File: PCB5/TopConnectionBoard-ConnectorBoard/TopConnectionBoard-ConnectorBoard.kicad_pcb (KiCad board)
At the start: 2 copper layers, 51 x 50 mm, 8 parts, among them P1 CONN1, P2 CONN2, P3 CONN_A, P4 CONN_B

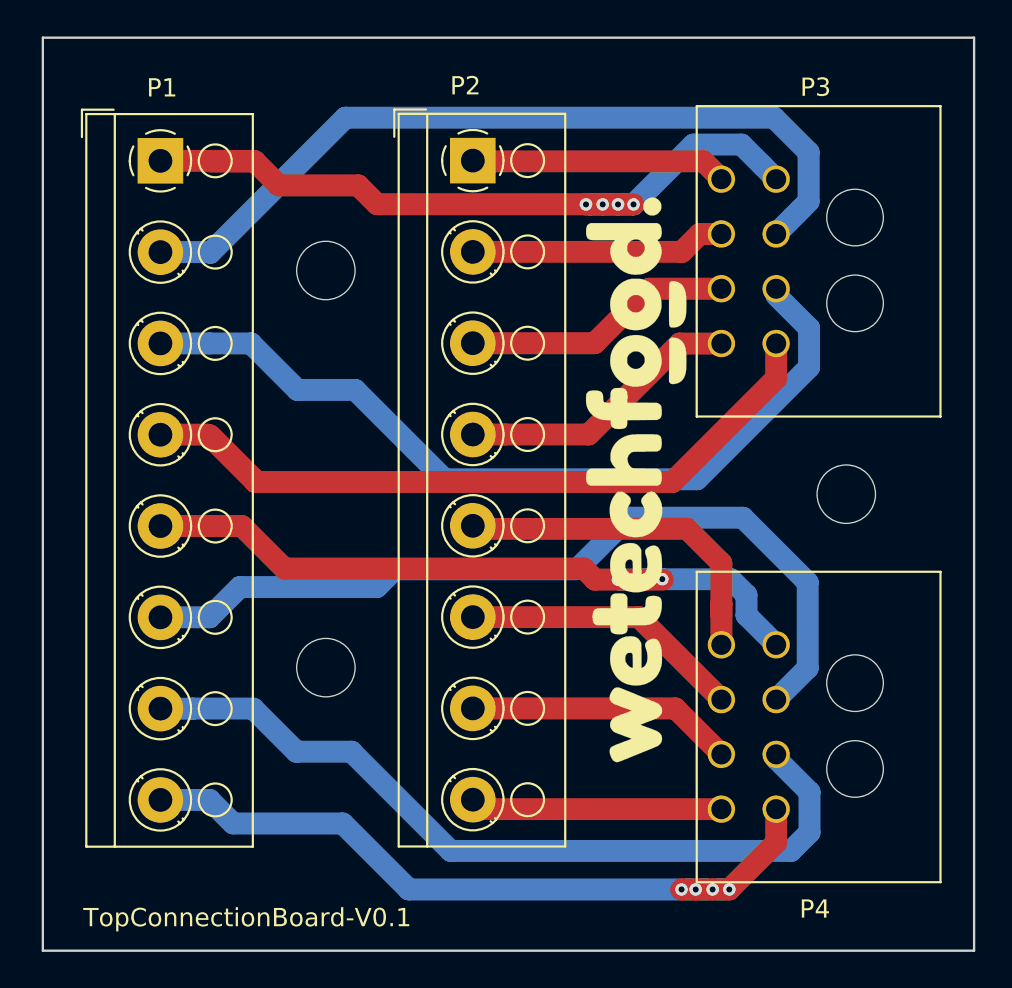
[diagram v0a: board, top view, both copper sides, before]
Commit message: Placa driver casi enrutada, step y medidas exportadas
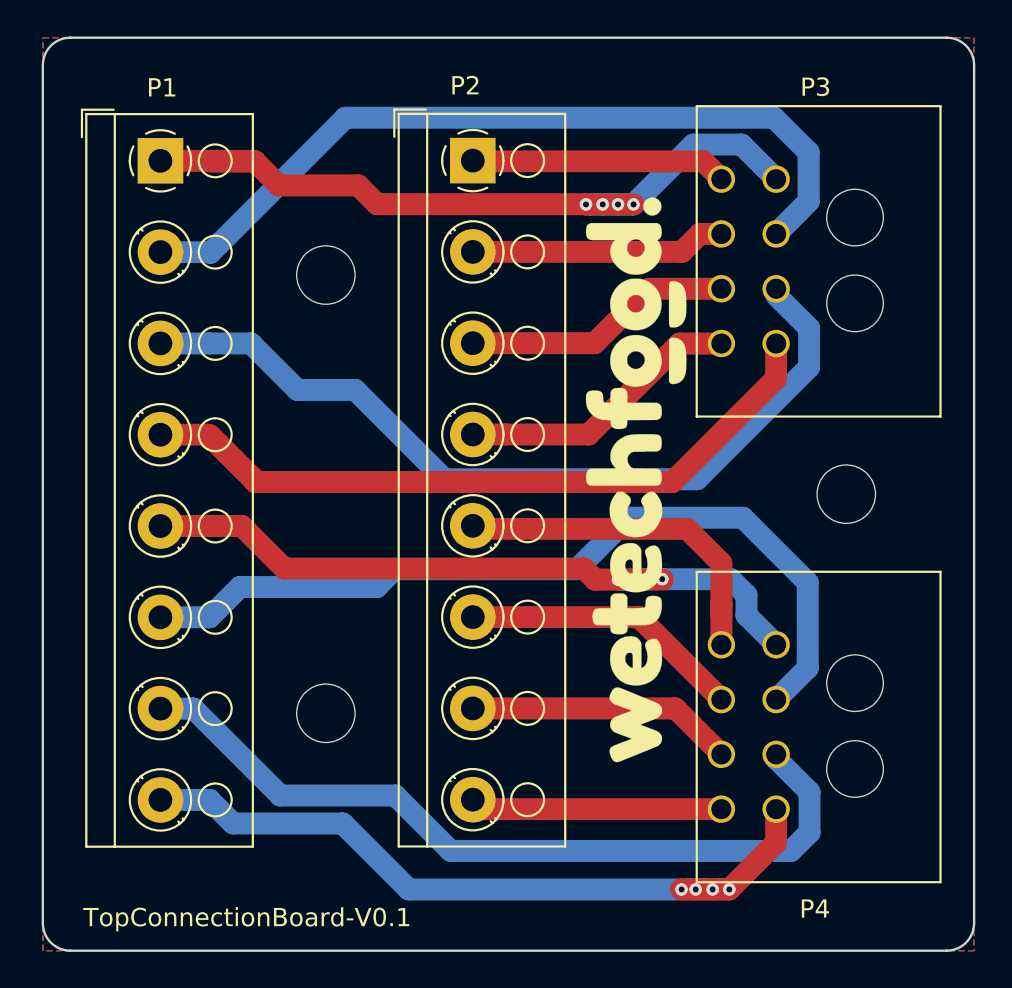
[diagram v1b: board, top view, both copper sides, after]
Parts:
- moved REF** 2.50 mm to (131.5, 122.0)
- moved REF** 0.25 mm to (131.5, 98.0)
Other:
- outline, holes or cut-outs redrawn
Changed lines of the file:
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@@
   (general
     (thickness 1.6)
-    (drawings 13)
+    (drawings 20)
     (tracks 126)
     (zones 0)
@@
   )
   (setup
-    (last_trace_width 1.2)
+    (last_trace_width 0.254)
     (user_trace_width 0.1524)
     (user_trace_width 0.2)
@@
     (visible_elements FFFFFF7F)
     (pcbplotparams
-      (layerselection 0x01100_7ffffffe)
+      (layerselection 0x010f0_ffffffff)
       (usegerberextensions true)
       (usegerberattributes true)
@@
       (excludeedgelayer true)
       (linewidth 0.127000)
-      (plotframeref true)
+      (plotframeref false)
       (viasonmask false)
       (mode 1)
@@
       (psnegative false)
       (psa4output false)
-      (plotreference false)
+      (plotreference true)
       (plotvalue false)
       (plotinvisibletext false)
       (padsonsilk false)
       (subtractmaskfromsilk false)
-      (outputformat 4)
+      (outputformat 1)
       (mirror false)
       (drillshape 0)
@@
   )
   (module Mounting_Holes:MountingHole_3.2mm_M3 (layer F.Cu)
-    (at 131.5 97.75)
+    (at 131.5 98)
     (descr "Mounting Hole 3.2mm, no annular, M3")
     (tags "mounting hole 3.2mm no annular m3")
@@
   )
   (module Mounting_Holes:MountingHole_3.2mm_M3 (layer F.Cu)
-    (at 131.5 119.5)
+    (at 131.5 122)
     (descr "Mounting Hole 3.2mm, no annular, M3")
     (tags "mounting hole 3.2mm no annular m3")
@@
     )
   )
-  (dimension 15.5 (width 0.15) (layer Dwgs.User)
-    (gr_text "15,500 mm" (at 113.2 127.25 270) (layer Dwgs.User)
-      (effects (font (size 1 1) (thickness 0.15)))
-    )
-    (feature1 (pts (xy 131.5 135) (xy 113.913579 135)))
-    (feature2 (pts (xy 131.5 119.5) (xy 113.913579 119.5)))
-    (crossbar (pts (xy 114.5 119.5) (xy 114.5 135)))
-    (arrow1a (pts (xy 114.5 135) (xy 113.913579 133.873496)))
-    (arrow1b (pts (xy 114.5 135) (xy 115.086421 133.873496)))
-    (arrow2a (pts (xy 114.5 119.5) (xy 113.913579 120.626504)))
-    (arrow2b (pts (xy 114.5 119.5) (xy 115.086421 120.626504)))
-  )
-  (dimension 21.75 (width 0.15) (layer Dwgs.User)
-    (gr_text "21,750 mm" (at 113.2 108.625 270) (layer Dwgs.User)
-      (effects (font (size 1 1) (thickness 0.15)))
-    )
-    (feature1 (pts (xy 131.5 119.5) (xy 113.913579 119.5)))
-    (feature2 (pts (xy 131.5 97.75) (xy 113.913579 97.75)))
-    (crossbar (pts (xy 114.5 97.75) (xy 114.5 119.5)))
-    (arrow1a (pts (xy 114.5 119.5) (xy 113.913579 118.373496)))
-    (arrow1b (pts (xy 114.5 119.5) (xy 115.086421 118.373496)))
-    (arrow2a (pts (xy 114.5 97.75) (xy 113.913579 98.876504)))
-    (arrow2b (pts (xy 114.5 97.75) (xy 115.086421 98.876504)))
-  )
-  (dimension 12.75 (width 0.15) (layer Dwgs.User)
-    (gr_text "12,750 mm" (at 113.2 91.375 90) (layer Dwgs.User)
-      (effects (font (size 1 1) (thickness 0.15)))
-    )
-    (feature1 (pts (xy 131.5 85) (xy 113.913579 85)))
-    (feature2 (pts (xy 131.5 97.75) (xy 113.913579 97.75)))
-    (crossbar (pts (xy 114.5 97.75) (xy 114.5 85)))
-    (arrow1a (pts (xy 114.5 85) (xy 115.086421 86.126504)))
-    (arrow1b (pts (xy 114.5 85) (xy 113.913579 86.126504)))
-    (arrow2a (pts (xy 114.5 97.75) (xy 115.086421 96.623496)))
-    (arrow2b (pts (xy 114.5 97.75) (xy 113.913579 96.623496)))
-  )
+  (dimension 28.5 (width 0.15) (layer Dwgs.User)
+    (gr_text "28,500 mm" (at 145.75 77.7) (layer Dwgs.User)
+      (effects (font (size 1 1) (thickness 0.15)))
+    )
+    (feature1 (pts (xy 160 110) (xy 160 78.413579)))
+    (feature2 (pts (xy 131.5 110) (xy 131.5 78.413579)))
+    (crossbar (pts (xy 131.5 79) (xy 160 79)))
+    (arrow1a (pts (xy 160 79) (xy 158.873496 79.586421)))
+    (arrow1b (pts (xy 160 79) (xy 158.873496 78.413579)))
+    (arrow2a (pts (xy 131.5 79) (xy 132.626504 79.586421)))
+    (arrow2b (pts (xy 131.5 79) (xy 132.626504 78.413579)))
+  )
+  (dimension 13 (width 0.15) (layer Dwgs.User)
+    (gr_text "13,000 mm" (at 112.2 128.5 270) (layer Dwgs.User)
+      (effects (font (size 1 1) (thickness 0.15)))
+    )
+    (feature1 (pts (xy 131.5 135) (xy 112.913579 135)))
+    (feature2 (pts (xy 131.5 122) (xy 112.913579 122)))
+    (crossbar (pts (xy 113.5 122) (xy 113.5 135)))
+    (arrow1a (pts (xy 113.5 135) (xy 112.913579 133.873496)))
+    (arrow1b (pts (xy 113.5 135) (xy 114.086421 133.873496)))
+    (arrow2a (pts (xy 113.5 122) (xy 112.913579 123.126504)))
+    (arrow2b (pts (xy 113.5 122) (xy 114.086421 123.126504)))
+  )
+  (dimension 13 (width 0.15) (layer Dwgs.User)
+    (gr_text "13,000 mm" (at 112.2 91.5 90) (layer Dwgs.User)
+      (effects (font (size 1 1) (thickness 0.15)))
+    )
+    (feature1 (pts (xy 131.5 85) (xy 112.913579 85)))
+    (feature2 (pts (xy 131.5 98) (xy 112.913579 98)))
+    (crossbar (pts (xy 113.5 98) (xy 113.5 85)))
+    (arrow1a (pts (xy 113.5 85) (xy 114.086421 86.126504)))
+    (arrow1b (pts (xy 113.5 85) (xy 112.913579 86.126504)))
+    (arrow2a (pts (xy 113.5 98) (xy 114.086421 96.873496)))
+    (arrow2b (pts (xy 113.5 98) (xy 112.913579 96.873496)))
+  )
+  (dimension 12 (width 0.15) (layer Dwgs.User)
+    (gr_text "12,000 mm" (at 112.2 116 90) (layer Dwgs.User)
+      (effects (font (size 1 1) (thickness 0.15)))
+    )
+    (feature1 (pts (xy 131.5 110) (xy 112.913579 110)))
+    (feature2 (pts (xy 131.5 122) (xy 112.913579 122)))
+    (crossbar (pts (xy 113.5 122) (xy 113.5 110)))
+    (arrow1a (pts (xy 113.5 110) (xy 114.086421 111.126504)))
+    (arrow1b (pts (xy 113.5 110) (xy 112.913579 111.126504)))
+    (arrow2a (pts (xy 113.5 122) (xy 114.086421 120.873496)))
+    (arrow2b (pts (xy 113.5 122) (xy 112.913579 120.873496)))
+  )
+  (dimension 12 (width 0.15) (layer Dwgs.User)
+    (gr_text "12,000 mm" (at 112.2 104 270) (layer Dwgs.User)
+      (effects (font (size 1 1) (thickness 0.15)))
+    )
+    (feature1 (pts (xy 131.5 110) (xy 112.913579 110)))
+    (feature2 (pts (xy 131.5 98) (xy 112.913579 98)))
+    (crossbar (pts (xy 113.5 98) (xy 113.5 110)))
+    (arrow1a (pts (xy 113.5 110) (xy 112.913579 108.873496)))
+    (arrow1b (pts (xy 113.5 110) (xy 114.086421 108.873496)))
+    (arrow2a (pts (xy 113.5 98) (xy 112.913579 99.126504)))
+    (arrow2b (pts (xy 113.5 98) (xy 114.086421 99.126504)))
+  )
+  (dimension 25 (width 0.15) (layer Dwgs.User)
+    (gr_text "25,000 mm" (at 173.8 122.5 270) (layer Dwgs.User)
+      (effects (font (size 1 1) (thickness 0.15)))
+    )
+    (feature1 (pts (xy 167 135) (xy 173.086421 135)))
+    (feature2 (pts (xy 167 110) (xy 173.086421 110)))
+    (crossbar (pts (xy 172.5 110) (xy 172.5 135)))
+    (arrow1a (pts (xy 172.5 135) (xy 171.913579 133.873496)))
+    (arrow1b (pts (xy 172.5 135) (xy 173.086421 133.873496)))
+    (arrow2a (pts (xy 172.5 110) (xy 171.913579 111.126504)))
+    (arrow2b (pts (xy 172.5 110) (xy 173.086421 111.126504)))
+  )
+  (gr_arc (start 117.5 133.5) (end 116 133.5) (angle -90) (layer Edge.Cuts) (width 0.127))
+  (gr_arc (start 117.5 86.5) (end 117.5 85) (angle -90) (layer Edge.Cuts) (width 0.127))
+  (gr_arc (start 165.5 133.5) (end 165.5 135) (angle -90) (layer Edge.Cuts) (width 0.127))
+  (gr_arc (start 165.5 86.5) (end 167 86.5) (angle -90) (layer Edge.Cuts) (width 0.127))
   (dimension 15.5 (width 0.15) (layer Dwgs.User)
     (gr_text "15,500 mm" (at 123.75 79.2) (layer Dwgs.User)
@@
     (arrow2b (pts (xy 168.5 85) (xy 169.086421 86.126504)))
   )
-  (gr_line (start 116 85) (end 167 85) (layer Edge.Cuts) (width 0.127))
-  (gr_line (start 116 135) (end 116 85) (layer Edge.Cuts) (width 0.127))
-  (gr_line (start 167 135) (end 116 135) (layer Edge.Cuts) (width 0.127))
-  (gr_line (start 167 85) (end 167 135) (layer Edge.Cuts) (width 0.127))
+  (gr_line (start 117.5 85) (end 165.5 85) (layer Edge.Cuts) (width 0.127))
+  (gr_line (start 116 133.5) (end 116 86.5) (layer Edge.Cuts) (width 0.127))
+  (gr_line (start 165.5 135) (end 117.5 135) (layer Edge.Cuts) (width 0.127))
+  (gr_line (start 167 86.5) (end 167 133.5) (layer Edge.Cuts) (width 0.127))
   (gr_text TopConnectionBoard-V0.1 (at 127.2032 133.1976) (layer F.SilkS)
     (effects (font (size 1 1) (thickness 0.2)))
@@
   (segment (start 151.6253 90.8558) (end 154.265 90.8558) (width 1.2) (layer B.Cu) (net 2))
   (segment (start 148.3487 94.1324) (end 151.6253 90.8558) (width 1.2) (layer B.Cu) (net 2))
+  (segment (start 156.1592 124.4854) (end 156.1592 124.25) (width 1.2) (layer B.Cu) (net 3))
   (segment (start 157.988 126.3142) (end 156.1592 124.4854) (width 1.2) (layer B.Cu) (net 3))
+  (segment (start 138.3411 129.54) (end 156.972 129.54) (width 1.2) (layer B.Cu) (net 3))
+  (segment (start 157.988 128.524) (end 157.988 126.3142) (width 1.2) (layer B.Cu) (net 3))
+  (segment (start 135.3011 126.5) (end 138.3411 129.54) (width 1.2) (layer B.Cu) (net 3))
   (segment (start 156.972 129.54) (end 157.988 128.524) (width 1.2) (layer B.Cu) (net 3))
-  (segment (start 138.3411 129.54) (end 156.972 129.54) (width 1.2) (layer B.Cu) (net 3))
-  (segment (start 132.9055 124.1044) (end 138.3411 129.54) (width 1.2) (layer B.Cu) (net 3))
-  (segment (start 129.8829 124.1044) (end 132.9055 124.1044) (width 1.2) (layer B.Cu) (net 3))
-  (segment (start 156.1592 124.4854) (end 156.1592 124.25) (width 1.2) (layer B.Cu) (net 3))
-  (segment (start 127.5207 121.7422) (end 129.8829 124.1044) (width 1.2) (layer B.Cu) (net 3))
-  (segment (start 124.211066 121.7422) (end 127.5207 121.7422) (width 1.2) (layer B.Cu) (net 3))
-  (segment (start 157.988 128.524) (end 157.988 126.3142) (width 1.2) (layer B.Cu) (net 3))
+  (segment (start 129 126.5) (end 135.3011 126.5) (width 1.2) (layer B.Cu) (net 3))
+  (segment (start 124.2422 121.7422) (end 129 126.5) (width 1.2) (layer B.Cu) (net 3))
+  (segment (start 124.211066 121.7422) (end 124.2422 121.7422) (width 1.2) (layer B.Cu) (net 3))
   (segment (start 124.208466 121.7448) (end 124.211066 121.7422) (width 1.2) (layer B.Cu) (net 3))
   (segment (start 122.4407 121.7448) (end 124.208466 121.7448) (width 1.2) (layer B.Cu) (net 3))
